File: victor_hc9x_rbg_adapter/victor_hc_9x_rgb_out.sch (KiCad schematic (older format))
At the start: 24 parts, among them J1 DB25_Female_MountingHoles, J2 SCART-F, J3 RIGHT, J4 DIN-8, J5 VIDEO, J6 LEFT, U1 ICL7660

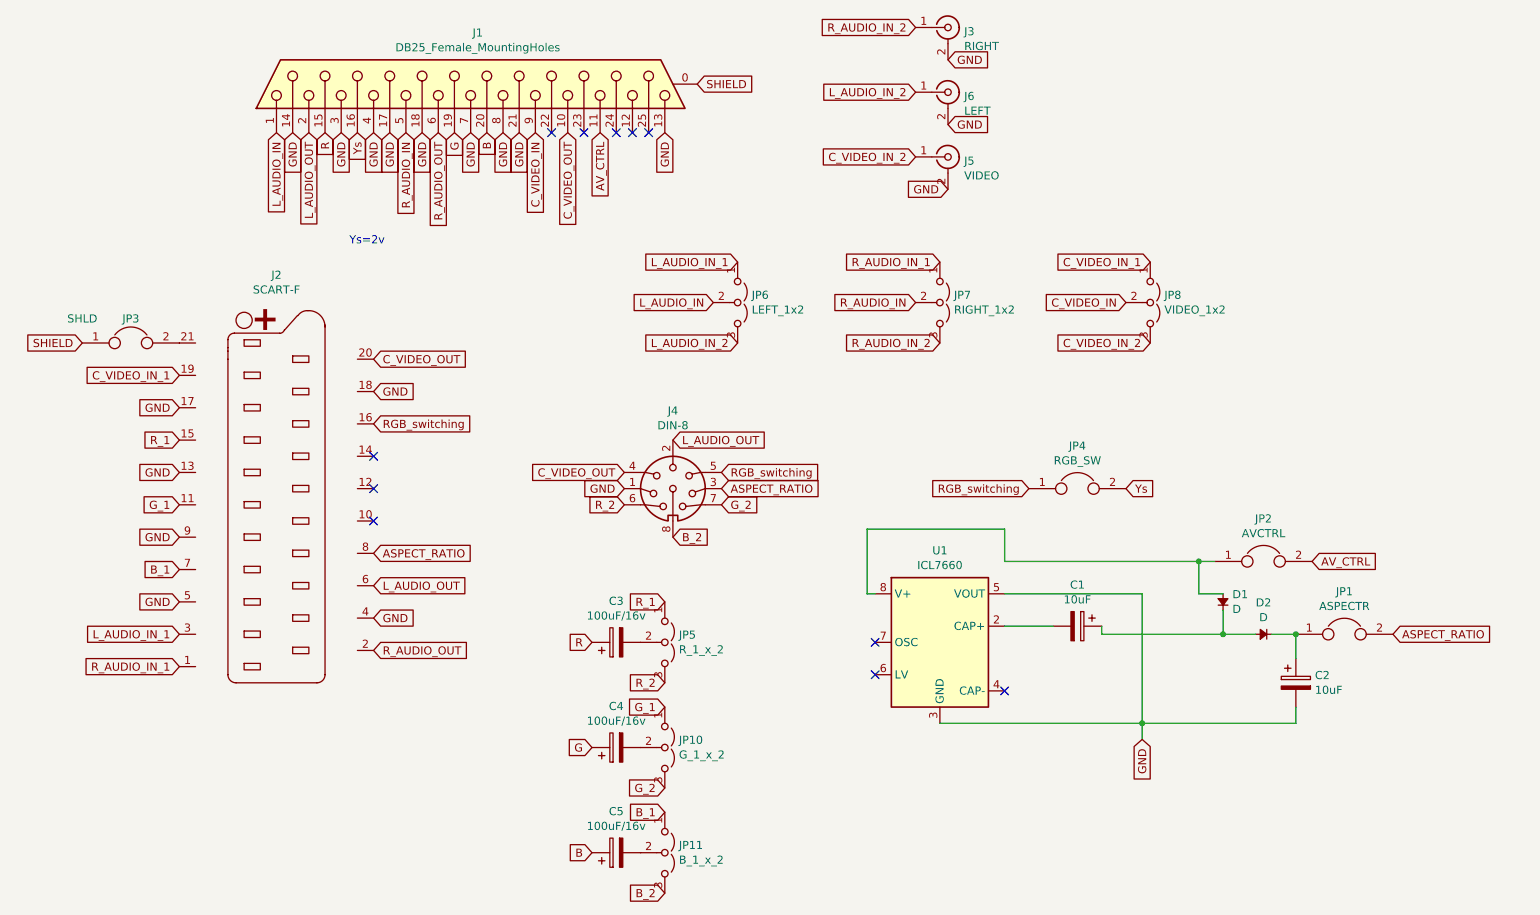
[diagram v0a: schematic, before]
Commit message: fixed din-8 footprint and scart connections
din-8 was mirrored, so now corrected. scart pins were not correct related to in and out audio/video. only rca audio/video input was correct towards db25 connector.
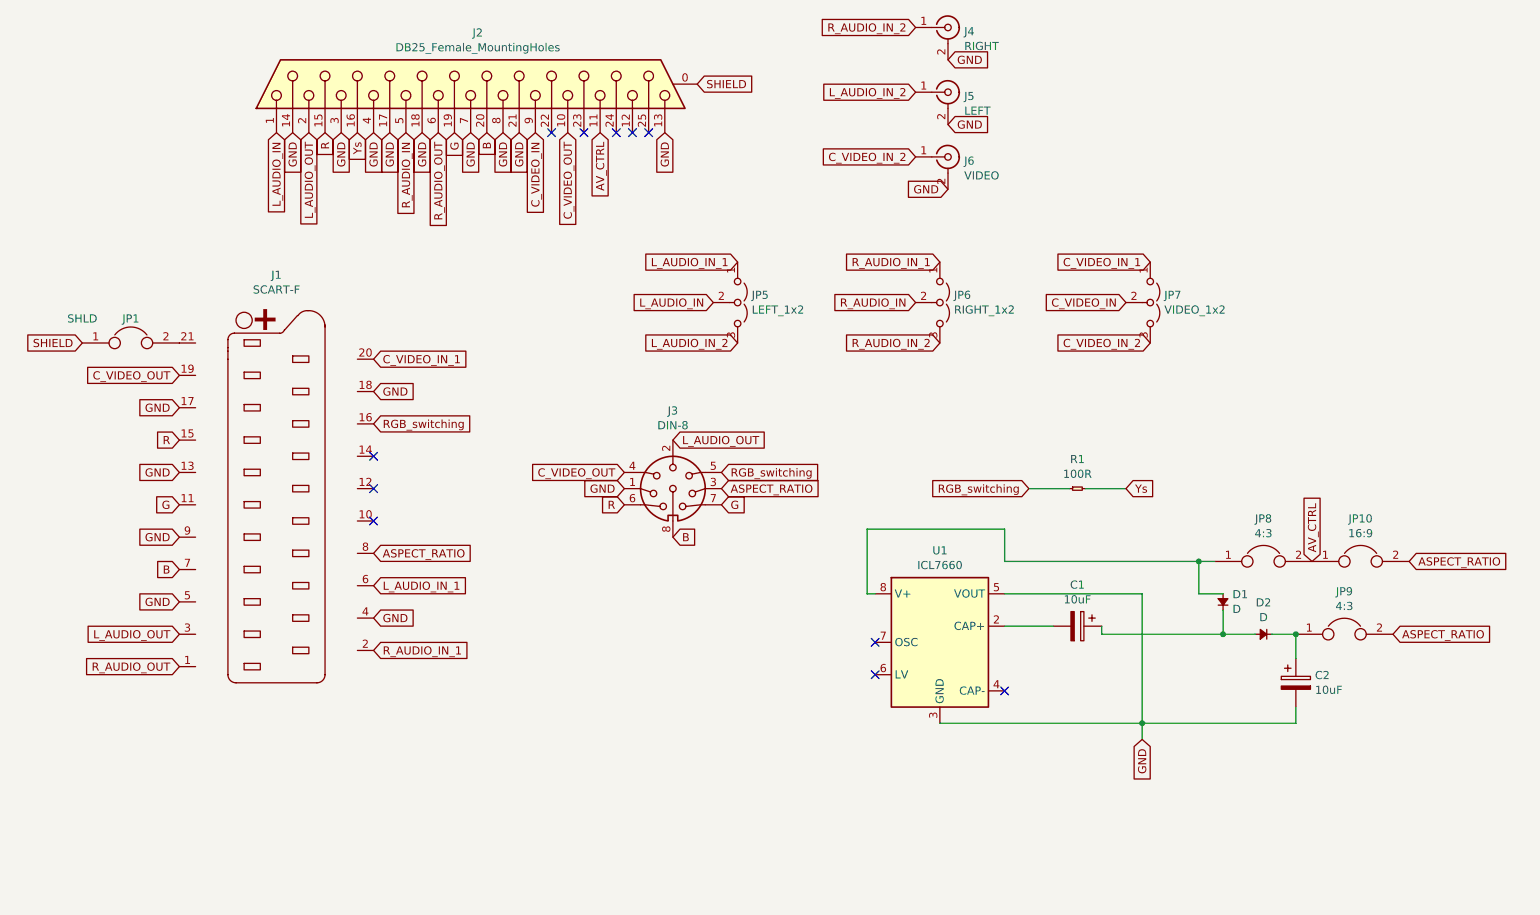
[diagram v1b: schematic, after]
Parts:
- removed C3, C4, C5: 100uF/16v, Capacitor_THT:CP_Radial_D8.0mm_P5.00mm, symbol Device:CP
- removed JP10: G_1_x_2, Connector_PinHeader_2.54mm:PinHeader_1x03_P2.54mm_Vertical, symbol Jumper:Jumper_3_Open
- removed JP11: B_1_x_2, Connector_PinHeader_2.54mm:PinHeader_1x03_P2.54mm_Vertical, symbol Jumper:Jumper_3_Open
- removed JP4: RGB_SW, Connector_PinHeader_2.54mm:PinHeader_1x02_P2.54mm_Vertical, symbol Device:Jumper
- removed JP5: R_1_x_2, Connector_PinHeader_2.54mm:PinHeader_1x03_P2.54mm_Vertical, symbol Jumper:Jumper_3_Open
- added JP10: 16:9, Connector_PinHeader_2.54mm:PinHeader_1x02_P2.54mm_Vertical, symbol Device:Jumper
- added R1: 100R, Resistor_THT:R_Axial_DIN0516_L15.5mm_D5.0mm_P7.62mm_Vertical, symbol agg-kicad:R
- JP8: renamed from JP2; value AVCTRL -> 4:3
- JP9: renamed from JP1; value ASPECTR -> 4:3
- renumbered J2 to J1, J1 to J2, J4 to J3, J3 to J4, J6 to J5, J5 to J6, JP3 to JP1, JP6 to JP5, JP7 to JP6, JP8 to JP7
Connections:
- net B_1 is gone; now on net B: J1.7 (P7)
- net B_2 is gone; now on net B: J3.8
- net G_1 is gone; now on net G: J1.11 (P11)
- net G_2 is gone; now on net G: J3.7
- net R_1 is gone; now on net R: J1.15 (P15)
- net R_2 is gone; now on net R: J3.6
- net ASPECT_RATIO: now also JP10.2
- net AV_CTRL: now also JP10.1
- net C_VIDEO_IN_1: now also J1.20 (P20); no longer J1.19 (P19)
- net C_VIDEO_OUT: now also J1.19 (P19); no longer J1.20 (P20)
- net L_AUDIO_IN_1: now also J1.6 (P6); no longer J1.3 (P3)
- net L_AUDIO_OUT: now also J1.3 (P3); no longer J1.6 (P6)
- net RGB_switching: now also R1.1
- net R_AUDIO_IN_1: now also J1.2 (P2); no longer J1.1 (P1)
- net R_AUDIO_OUT: now also J1.1 (P1); no longer J1.2 (P2)
- net Ys: now also R1.2
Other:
- note removed: "Ys=2v"
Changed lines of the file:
@@
 $EndDescr
 $Comp
-L Connector:SCART-F J2
+L Connector:SCART-F J1
 U 1 1 62A8E208
 P 2100 4200
-F 0 "J2" H 2100 5620 50  0000 C CNN
+F 0 "J1" H 2100 5620 50  0000 C CNN
 F 1 "SCART-F" H 2100 5529 50  0000 C CNN
 F 2 "Connector_Coaxial:SCART" H 2100 4250 50  0001 C CNN
@@
 $EndComp
 $Comp
-L Connector:DB25_Female_MountingHoles J1
+L Connector:DB25_Female_MountingHoles J2
 U 1 1 62A8F49C
 P 3300 1600
-F 0 "J1" V 3617 1556 50  0000 C CNN
+F 0 "J2" V 3617 1556 50  0000 C CNN
 F 1 "DB25_Female_MountingHoles" V 3526 1556 50  0000 C CNN
 F 2 "Connector_Dsub:DSUB-25_Female_Horizontal_P2.77x2.84mm_EdgePinOffset9.90mm_Housed_MountingHolesOffset11.32mm" H 3300 1600 50  0001 C CNN
@@
 GND
 NoConn ~ 4300 1900
-Text Notes 2550 2600 0    50   ~ 0
-Ys=2v
-$Comp
-L Device:Jumper JP2
+$Comp
+L Device:Jumper JP8
 U 1 1 62BCCD46
 P 8200 4550
-F 0 "JP2" H 8200 4814 50  0000 C CNN
-F 1 "AVCTRL" H 8200 4723 50  0000 C CNN
+F 0 "JP8" H 8200 4814 50  0000 C CNN
+F 1 "4:3" H 8200 4723 50  0000 C CNN
 F 2 "Connector_PinHeader_2.54mm:PinHeader_1x02_P2.54mm_Vertical" H 8200 4550 50  0001 C CNN
 F 3 "~" H 8200 4550 50  0001 C CNN
@@
 Text GLabel 2700 3500 2    50   Input ~ 0
 GND
-Text GLabel 2700 4700 2    50   Input ~ 0
+Text GLabel 1500 5000 0    50   Input ~ 0
 L_AUDIO_OUT
-Text GLabel 2700 5100 2    50   Input ~ 0
+Text GLabel 1500 5200 0    50   Input ~ 0
 R_AUDIO_OUT
-Text GLabel 2700 3300 2    50   Input ~ 0
+Text GLabel 1500 3400 0    50   Input ~ 0
 C_VIDEO_OUT
 NoConn ~ 2700 4100
@@
 GND
 $Comp
-L Device:Jumper JP3
+L Device:Jumper JP1
 U 1 1 62BDE10C
 P 1200 3200
-F 0 "JP3" H 1200 3350 50  0000 C CNN
+F 0 "JP1" H 1200 3350 50  0000 C CNN
 F 1 "SHLD" H 900 3350 50  0000 C CNN
 F 2 "Connector_PinHeader_2.54mm:PinHeader_1x02_P2.54mm_Vertical" H 1200 3200 50  0001 C CNN
@@
 $EndComp
 Text GLabel 1500 4600 0    50   Input ~ 0
-B_1
+B
 Text GLabel 1500 4200 0    50   Input ~ 0
-G_1
+G
 Text GLabel 1500 3800 0    50   Input ~ 0
-R_1
-Text GLabel 1500 5200 0    50   Input ~ 0
+R
+Text GLabel 2700 5100 2    50   Input ~ 0
 R_AUDIO_IN_1
-Text GLabel 1500 5000 0    50   Input ~ 0
+Text GLabel 2700 4700 2    50   Input ~ 0
 L_AUDIO_IN_1
-Text GLabel 1500 3400 0    50   Input ~ 0
+Text GLabel 2700 3300 2    50   Input ~ 0
 C_VIDEO_IN_1
 $Comp
-L Jumper:Jumper_3_Open JP6
+L Jumper:Jumper_3_Open JP5
 U 1 1 62BF2479
 P 4950 2950
-F 0 "JP6" V 4904 3037 50  0000 L CNN
+F 0 "JP5" V 4904 3037 50  0000 L CNN
 F 1 "LEFT_1x2" V 4995 3037 50  0000 L CNN
 F 2 "Connector_PinHeader_2.54mm:PinHeader_1x03_P2.54mm_Vertical" H 4950 2950 50  0001 C CNN
@@
 L_AUDIO_IN
 $Comp
-L Jumper:Jumper_3_Open JP7
+L Jumper:Jumper_3_Open JP6
 U 1 1 62BF95B0
 P 6200 2950
-F 0 "JP7" V 6154 3037 50  0000 L CNN
+F 0 "JP6" V 6154 3037 50  0000 L CNN
 F 1 "RIGHT_1x2" V 6245 3037 50  0000 L CNN
 F 2 "Connector_PinHeader_2.54mm:PinHeader_1x03_P2.54mm_Vertical" H 6200 2950 50  0001 C CNN
@@
 R_AUDIO_IN
 $Comp
-L Jumper:Jumper_3_Open JP8
+L Jumper:Jumper_3_Open JP7
 U 1 1 62C13E9D
 P 7500 2950
-F 0 "JP8" V 7454 3037 50  0000 L CNN
+F 0 "JP7" V 7454 3037 50  0000 L CNN
 F 1 "VIDEO_1x2" V 7545 3037 50  0000 L CNN
 F 2 "Connector_PinHeader_2.54mm:PinHeader_1x03_P2.54mm_Vertical" H 7500 2950 50  0001 C CNN
@@
 C_VIDEO_IN_2
 $Comp
-L Connector:DIN-8 J4
+L Connector:DIN-8 J3
 U 1 1 62C18397
 P 4550 4100
-F 0 "J4" H 4550 4581 50  0000 C CNN
+F 0 "J3" H 4550 4581 50  0000 C CNN
 F 1 "DIN-8" H 4550 4490 50  0000 C CNN
 F 2 "Connector_DIN:din8_msx" H 4550 4100 50  0001 C CNN
@@
 Text GLabel 7350 4100 2    50   Input ~ 0
 Ys
-$Comp
-L Device:Jumper JP4
-U 1 1 62C1E45A
-P 7050 4100
-F 0 "JP4" H 7050 4364 50  0000 C CNN
-F 1 "RGB_SW" H 7050 4273 50  0000 C CNN
-F 2 "Connector_PinHeader_2.54mm:PinHeader_1x02_P2.54mm_Vertical" H 7050 4100 50  0001 C CNN
-F 3 "~" H 7050 4100 50  0001 C CNN
-	1    7050 4100
-	1    0    0    -1
-$EndComp
-Text GLabel 8500 4550 2    50   Input ~ 0
+Text GLabel 8500 4550 1    50   Input ~ 0
 AV_CTRL
 Text GLabel 4250 4000 0    50   Input ~ 0
 C_VIDEO_OUT
 Text GLabel 4250 4200 0    50   Input ~ 0
-R_2
+R
 Text GLabel 4850 4200 2    50   Input ~ 0
-G_2
+G
 Text GLabel 4550 4400 2    50   Input ~ 0
-B_2
+B
 $Comp
 L Regulator_SwitchedCapacitor:ICL7660 U1
@@
 ASPECT_RATIO
 $Comp
-L Connector:Conn_Coaxial J5
+L Connector:Conn_Coaxial J6
 U 1 1 62C758A1
 P 6250 2050
-F 0 "J5" H 6350 2025 50  0000 L CNN
+F 0 "J6" H 6350 2025 50  0000 L CNN
 F 1 "VIDEO" H 6350 1934 50  0000 L CNN
 F 2 "Connector_Audio:rca_audio" H 6250 2050 50  0001 C CNN
@@
 ASPECT_RATIO
 $Comp
-L Device:Jumper JP1
+L Device:Jumper JP9
 U 1 1 62CAB7AB
 P 8700 5000
-F 0 "JP1" H 8700 5264 50  0000 C CNN
-F 1 "ASPECTR" H 8700 5173 50  0000 C CNN
+F 0 "JP9" H 8700 5264 50  0000 C CNN
+F 1 "4:3" H 8700 5173 50  0000 C CNN
 F 2 "Connector_PinHeader_2.54mm:PinHeader_1x02_P2.54mm_Vertical" H 8700 5000 50  0001 C CNN
 F 3 "~" H 8700 5000 50  0001 C CNN
@@
 NoConn ~ 5800 5250
 NoConn ~ 6600 5350
-Text GLabel 4050 5050 0    50   Input ~ 0
-R
-$Comp
-L Device:CP C3
-U 1 1 62CBBD93
-P 4200 5050
-F 0 "C3" V 4455 5050 50  0000 C CNN
-F 1 "100uF/16v" V 4364 5050 50  0000 C CNN
-F 2 "Capacitor_THT:CP_Radial_D8.0mm_P5.00mm" H 4238 4900 50  0001 C CNN
-F 3 "~" H 4200 5050 50  0001 C CNN
-	1    4200 5050
-	0    -1   -1   0
-$EndComp
-$Comp
-L Jumper:Jumper_3_Open JP5
-U 1 1 62CCA51A
-P 4500 5050
-F 0 "JP5" V 4454 5137 50  0000 L CNN
-F 1 "R_1_x_2" V 4545 5137 50  0000 L CNN
-F 2 "Connector_PinHeader_2.54mm:PinHeader_1x03_P2.54mm_Vertical" H 4500 5050 50  0001 C CNN
-F 3 "~" H 4500 5050 50  0001 C CNN
-	1    4500 5050
-	0    1    1    0
-$EndComp
-Text GLabel 4500 4800 0    50   Input ~ 0
-R_1
-Text GLabel 4500 5300 0    50   Input ~ 0
-R_2
-Text GLabel 4050 5700 0    50   Input ~ 0
-G
-$Comp
-L Device:CP C4
-U 1 1 62CE8F59
-P 4200 5700
-F 0 "C4" V 4455 5700 50  0000 C CNN
-F 1 "100uF/16v" V 4364 5700 50  0000 C CNN
-F 2 "Capacitor_THT:CP_Radial_D8.0mm_P5.00mm" H 4238 5550 50  0001 C CNN
-F 3 "~" H 4200 5700 50  0001 C CNN
-	1    4200 5700
-	0    -1   -1   0
-$EndComp
-$Comp
-L Jumper:Jumper_3_Open JP10
-U 1 1 62CE8F5F
-P 4500 5700
-F 0 "JP10" V 4454 5787 50  0000 L CNN
-F 1 "G_1_x_2" V 4545 5787 50  0000 L CNN
-F 2 "Connector_PinHeader_2.54mm:PinHeader_1x03_P2.54mm_Vertical" H 4500 5700 50  0001 C CNN
-F 3 "~" H 4500 5700 50  0001 C CNN
-	1    4500 5700
-	0    1    1    0
-$EndComp
-Text GLabel 4500 5450 0    50   Input ~ 0
-G_1
-Text GLabel 4500 5950 0    50   Input ~ 0
-G_2
-Text GLabel 4050 6350 0    50   Input ~ 0
-B
-$Comp
-L Device:CP C5
-U 1 1 62CE9A43
-P 4200 6350
-F 0 "C5" V 4455 6350 50  0000 C CNN
-F 1 "100uF/16v" V 4364 6350 50  0000 C CNN
-F 2 "Capacitor_THT:CP_Radial_D8.0mm_P5.00mm" H 4238 6200 50  0001 C CNN
-F 3 "~" H 4200 6350 50  0001 C CNN
-	1    4200 6350
-	0    -1   -1   0
-$EndComp
-$Comp
-L Jumper:Jumper_3_Open JP11
-U 1 1 62CE9A49
-P 4500 6350
-F 0 "JP11" V 4454 6437 50  0000 L CNN
-F 1 "B_1_x_2" V 4545 6437 50  0000 L CNN
-F 2 "Connector_PinHeader_2.54mm:PinHeader_1x03_P2.54mm_Vertical" H 4500 6350 50  0001 C CNN
-F 3 "~" H 4500 6350 50  0001 C CNN
-	1    4500 6350
-	0    1    1    0
-$EndComp
-Text GLabel 4500 6100 0    50   Input ~ 0
-B_1
-Text GLabel 4500 6600 0    50   Input ~ 0
-B_2
-$Comp
-L Connector:Conn_Coaxial J3
+$Comp
+L Connector:Conn_Coaxial J4
 U 1 1 62B7510F
 P 6250 1250
-F 0 "J3" H 6350 1225 50  0000 L CNN
+F 0 "J4" H 6350 1225 50  0000 L CNN
 F 1 "RIGHT" H 6350 1134 50  0000 L CNN
 F 2 "Connector_Audio:rca_audio" H 6250 1250 50  0001 C CNN
@@
 $EndComp
 $Comp
-L Connector:Conn_Coaxial J6
+L Connector:Conn_Coaxial J5
 U 1 1 62B755B6
 P 6250 1650
-F 0 "J6" H 6350 1625 50  0000 L CNN
+F 0 "J5" H 6350 1625 50  0000 L CNN
 F 1 "LEFT" H 6350 1534 50  0000 L CNN
 F 2 "Connector_Audio:rca_audio" H 6250 1650 50  0001 C CNN
@@
 Text GLabel 900  3200 0    50   Input ~ 0
 SHIELD
+$Comp
+L agg-kicad:R R1
+U 1 1 62E5DBFE
+P 7000 4100
+F 0 "R1" H 7050 4281 50  0000 C CNN
+F 1 "100R" H 7050 4190 50  0000 C CNN
+F 2 "Resistor_THT:R_Axial_DIN0516_L15.5mm_D5.0mm_P7.62mm_Vertical" H 7000 4100 50  0001 C CNN
+F 3 "" H 7000 4100 50  0001 C CNN
+	1    7000 4100
+	1    0    0    -1
+$EndComp
+Wire Wire Line
+	6750 4100 7000 4100
+Wire Wire Line
+	7100 4100 7350 4100
+Text GLabel 9100 4550 2    50   Input ~ 0
+ASPECT_RATIO
+$Comp
+L Device:Jumper JP10
+U 1 1 62E70AE6
+P 8800 4550
+F 0 "JP10" H 8800 4814 50  0000 C CNN
+F 1 "16:9" H 8800 4723 50  0000 C CNN
+F 2 "Connector_PinHeader_2.54mm:PinHeader_1x02_P2.54mm_Vertical" H 8800 4550 50  0001 C CNN
+F 3 "~" H 8800 4550 50  0001 C CNN
+	1    8800 4550
+	1    0    0    -1
+$EndComp
 $EndSCHEMATC
